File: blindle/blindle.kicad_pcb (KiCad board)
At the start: 2 copper layers, 21 parts, among them J1 CONN_5V, J2 CONN_8V, M1 74HC595, P1 pololua4988, P2 pololua4988, P3 pololua4988, P4 pololua4988, P5 pololua4988, P6 pololua4988, P7 pololua4988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

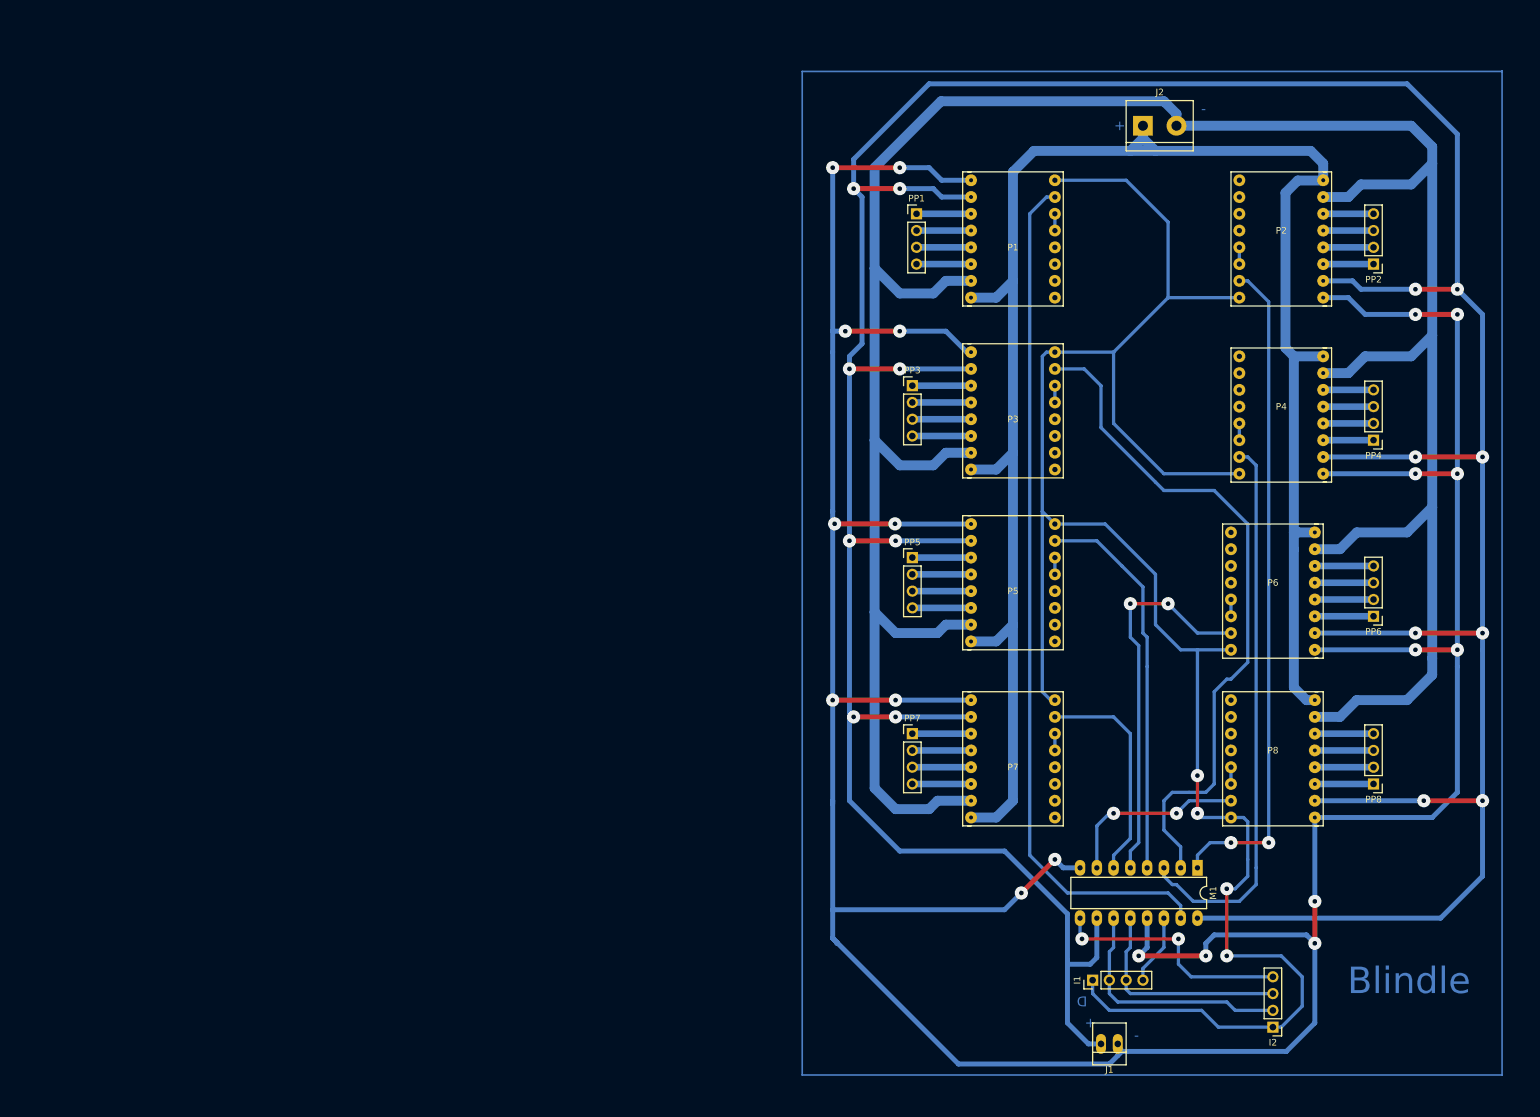
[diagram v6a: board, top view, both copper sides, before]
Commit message: version para placa mas chica
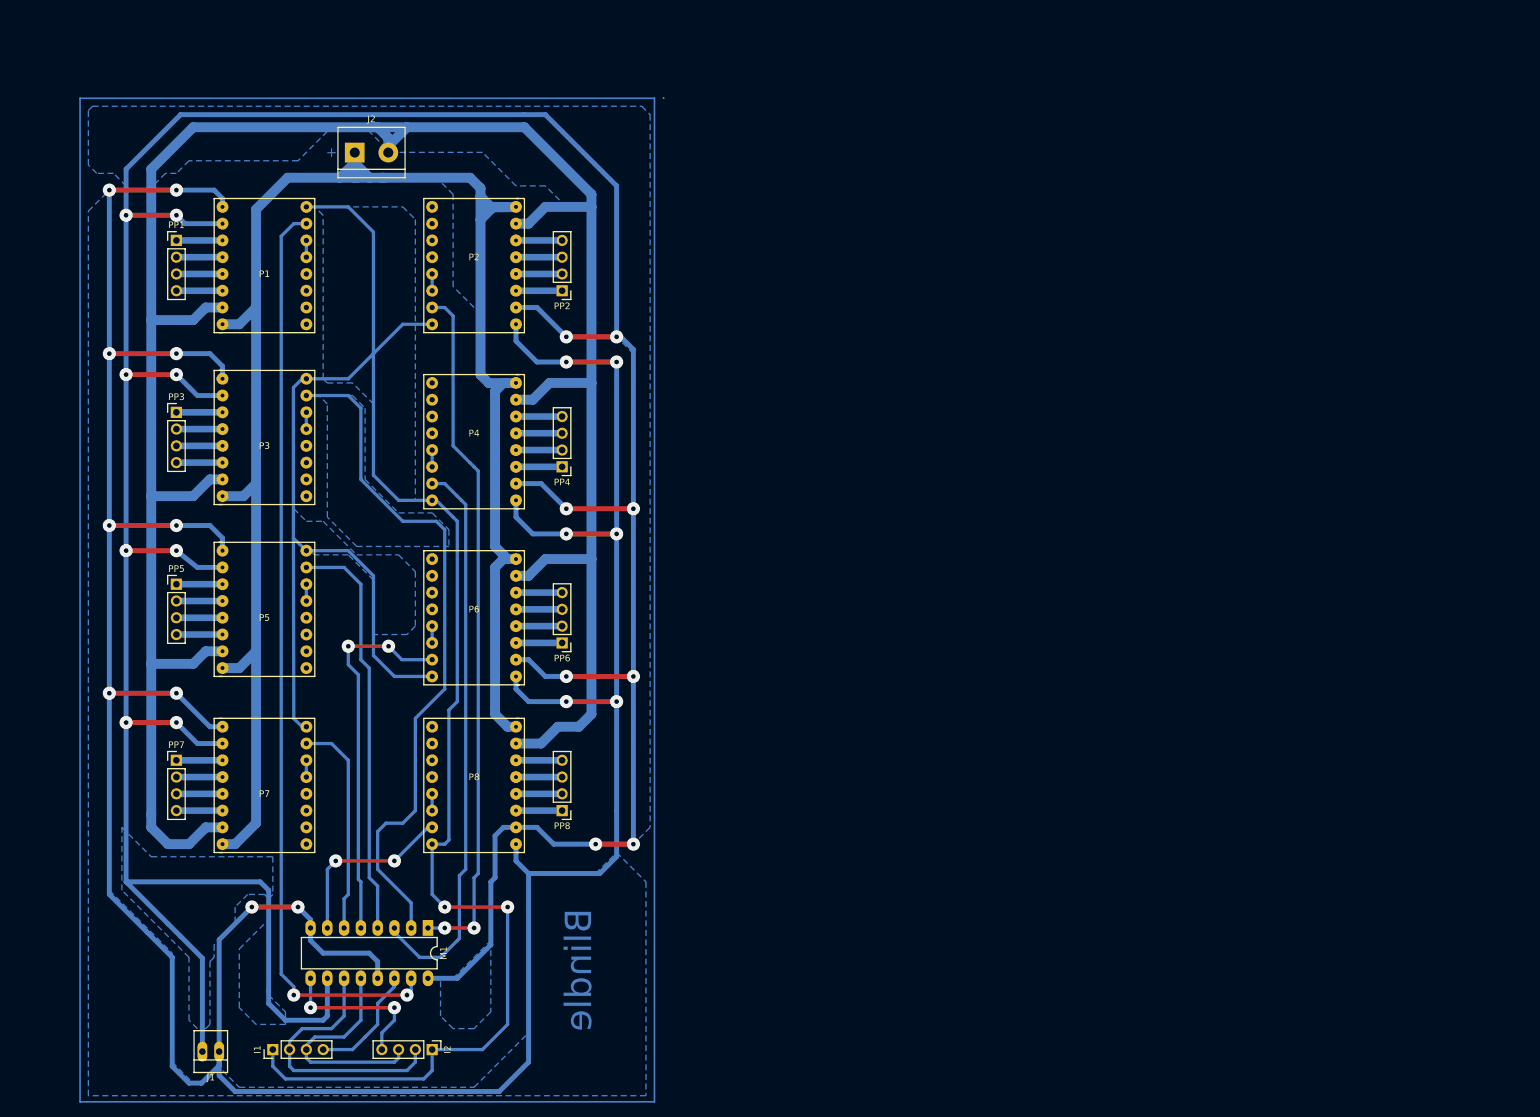
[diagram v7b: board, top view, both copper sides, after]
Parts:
- moved J1 136.1 mm to (68.1, 172.4)
- moved I2 127.4 mm to (100.3, 172.1), turned to 270 degrees
- moved I1 124.6 mm to (76.2, 172.1)
- moved PP2 123.0 mm to (120.0, 57.1)
- moved PP4 123.0 mm to (120.0, 83.8)
- moved PP6 123.0 mm to (120.0, 110.5)
- moved PP8 123.0 mm to (120.0, 135.9)
- moved P2 122.3 mm to (100.3, 44.5)
- moved P4 122.3 mm to (100.3, 71.1)
- moved P6 121.1 mm to (100.3, 97.8)
- moved P8 121.1 mm to (100.3, 123.2)
- moved J2 119.4 mm to (88.6, 36.2)
- moved M1 116.9 mm to (99.7, 153.7)
- moved P1 113.4 mm to (81.3, 62.2)
- moved P3 113.4 mm to (81.3, 88.3)
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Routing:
- net +5V: track 605.5 -> 545.6 mm
- net GNDD: track 411.7 -> 360.7 mm
- net GND: track 557.7 -> 509.7 mm, vias 20 -> 16
- net (no net): track 516.1 -> 478.1 mm
- net Net-(I2-Pad4): track 36.8 -> 24.3 mm
- net Net-(M1-Pad15): track 129.9 -> 140.3 mm, vias 0 -> 2
- net dir: track 302.4 -> 311.8 mm, vias 4 -> 2
- net Net-(I1-Pad4): track 11.9 -> 18.5 mm
- net Net-(M1-Pad1): track 101.2 -> 105.2 mm
- net Net-(M1-Pad4): track 59.0 -> 62.4 mm
- net +8V: track 278.6 -> 275.5 mm
- net Net-(I1-Pad2): track 38.7 -> 41.7 mm
- net Net-(P8-Pad14): track 8.89 -> 6.98 mm
- net Net-(P8-Pad13): track 8.89 -> 6.98 mm
- net Net-(P8-Pad12): track 8.89 -> 6.98 mm
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- added copper zone on B.Cu, net +5V
- added copper zone on B.Cu, net +8V
- added copper zone on B.Cu, net GND
- added copper zone on B.Cu, net GNDD
- added copper zone on B.Cu, net Net-(M1-Pad2)
- added copper zone on B.Cu, net dir
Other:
- board text removed: "-"
- board text removed: "D"

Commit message: cambios menores
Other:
- board text added: "+5v"
- board text added: "+8v"
- board text added: "CK"
- board text added: "DATA"
- board text added: "DATA'"
- board text added: "Dir"
- board text added: "GND"
- board text added: "GNDD"
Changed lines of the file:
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@@
     (area 46.674999 27.644999 135.705002 180.325002)
     (thickness 1.6)
-    (drawings 6)
+    (drawings 24)
     (tracks 454)
     (zones 0)
@@
     (41 Cmts.User user)
     (42 Eco1.User user)
-    (43 Eco2.User user)
-    (44 Edge.Cuts user)
+    (43 Eco2.User user hide)
+    (44 Edge.Cuts user hide)
     (45 Margin user)
-    (46 B.CrtYd user)
+    (46 B.CrtYd user hide)
     (47 F.CrtYd user hide)
     (48 B.Fab user)
@@
     (pad_to_mask_clearance 0.2)
     (aux_axis_origin 0 0)
-    (visible_elements 7FFFFFFF)
+    (visible_elements 7FFCFFFF)
     (pcbplotparams
       (layerselection 0x00030_80000001)
@@
       (net 10 GND))
   )
+  (gr_line (start 47 28) (end 47 180) (angle 90) (layer B.Adhes) (width 0.2))
+  (gr_line (start 134 28) (end 47 28) (angle 90) (layer B.Adhes) (width 0.2))
+  (gr_line (start 134 180) (end 134 28) (angle 90) (layer B.Adhes) (width 0.2))
+  (gr_line (start 47 180) (end 134 180) (angle 90) (layer B.Adhes) (width 0.2))
+  (gr_circle (center 128.778 33.274) (end 124.714 34.544) (layer F.Adhes) (width 0.5))
+  (gr_circle (center 52.578 33.274) (end 50.038 30.226) (layer F.Adhes) (width 0.5))
+  (gr_text +8v (at 83.82 36.195 90) (layer B.Adhes)
+    (effects (font (size 1.5 1.5) (thickness 0.3)) (justify mirror))
+  )
+  (gr_text GNDD (at 98.425 35.56 90) (layer B.Adhes)
+    (effects (font (size 1.5 1.5) (thickness 0.3)) (justify mirror))
+  )
+  (gr_text "GND\n" (at 62.865 172.085 90) (layer B.Adhes)
+    (effects (font (size 1.5 1.5) (thickness 0.3)) (justify mirror))
+  )
+  (gr_text +5v (at 70.485 172.085 90) (layer B.Adhes)
+    (effects (font (size 1.5 1.5) (thickness 0.3)) (justify mirror))
+  )
+  (gr_text CK (at 95.25 175.26 90) (layer B.Adhes)
+    (effects (font (size 1.5 1.5) (thickness 0.3)) (justify mirror))
+  )
+  (gr_text Dir (at 100.33 175.26 90) (layer B.Adhes)
+    (effects (font (size 1.5 1.5) (thickness 0.3)) (justify mirror))
+  )
+  (gr_text CK (at 81.28 175.26 90) (layer B.Adhes)
+    (effects (font (size 1.5 1.5) (thickness 0.3)) (justify mirror))
+  )
+  (gr_text CK (at 78.74 175.26 90) (layer B.Adhes)
+    (effects (font (size 1.5 1.5) (thickness 0.3)) (justify mirror))
+  )
+  (gr_text DATA' (at 92.71 176.53 90) (layer B.Adhes)
+    (effects (font (size 1.5 1.5) (thickness 0.3)) (justify mirror))
+  )
+  (gr_text DATA (at 83.82 176.53 90) (layer B.Adhes)
+    (effects (font (size 1.5 1.5) (thickness 0.3)) (justify mirror))
+  )
+  (gr_text CK (at 97.79 175.26 90) (layer B.Adhes)
+    (effects (font (size 1.5 1.5) (thickness 0.3)) (justify mirror))
+  )
+  (gr_text Dir (at 76.2 175.26 90) (layer B.Adhes)
+    (effects (font (size 1.5 1.5) (thickness 0.3)) (justify mirror))
+  )
   (gr_text + (at 85.09 36.195) (layer B.Cu)
     (effects (font (size 1.5 1.5) (thickness 0.3)) (justify mirror))
@@
     (effects (font (size 4 4) (thickness 1)) (justify mirror))
   )
-  (gr_circle (center 128.84 33.27) (end 130.84 32.27) (layer B.Adhes) (width 1))
-  (gr_circle (center 52.43 33.27) (end 50.43 32.27) (layer B.Adhes) (width 1))
-  (gr_circle (center 52.43 174.73) (end 50.43 175.73) (layer B.Adhes) (width 1))
-  (gr_circle (center 128.84 174.73) (end 127.84 176.73) (layer B.Adhes) (width 1))
+  (gr_circle (center 128.84 33.27) (end 130.84 32.27) (layer F.Adhes) (width 1))
+  (gr_circle (center 52.43 33.27) (end 50.43 32.27) (layer F.Adhes) (width 1))
+  (gr_circle (center 52.43 174.73) (end 50.43 175.73) (layer F.Adhes) (width 1))
+  (gr_circle (center 128.84 174.73) (end 127.84 176.73) (layer F.Adhes) (width 1))
   (segment (start 47 180) (end 134 180) (width 0.25) (layer B.Cu) (net 0))
   (segment (start 47 28) (end 47 180) (width 0.25) (layer B.Cu) (net 0))
@@
     )
   )
-  (zone (net 0) (net_name "") (layer B.Cu) (hatch edge 0.508)
-    (connect_pads (clearance 0.508))
-    (min_thickness 0.254)
-    (keepout (tracks not_allowed) (vias not_allowed) (copperpour not_allowed))
-    (fill (arc_segments 16) (thermal_gap 0.508) (thermal_bridge_width 0.508))
-    (polygon
-      (pts
-        (xy 54.61 34.925) (xy 50.165 34.925) (xy 50.165 31.75) (xy 54.61 31.75)
-      )
-    )
-  )
-  (zone (net 0) (net_name "") (layer B.Cu) (hatch edge 0.508)
-    (connect_pads (clearance 0.508))
-    (min_thickness 0.254)
-    (keepout (tracks not_allowed) (vias not_allowed) (copperpour not_allowed))
-    (fill (arc_segments 16) (thermal_gap 0.508) (thermal_bridge_width 0.508))
-    (polygon
-      (pts
-        (xy 130.81 35.306) (xy 127 35.306) (xy 127 31.496) (xy 130.81 31.496)
-      )
-    )
-  )
-  (zone (net 0) (net_name "") (layer B.Cu) (hatch edge 0.508)
-    (connect_pads (clearance 0.508))
-    (min_thickness 0.254)
-    (keepout (tracks not_allowed) (vias not_allowed) (copperpour not_allowed))
-    (fill (arc_segments 16) (thermal_gap 0.508) (thermal_bridge_width 0.508))
-    (polygon
-      (pts
-        (xy 130.81 176.53) (xy 127 176.53) (xy 127 172.72) (xy 130.81 172.72)
-      )
-    )
-  )
   (zone (net 6) (net_name +5V) (layer B.Cu) (hatch edge 0.508)
     (connect_pads (clearance 0.508))
@@
       )
     )
+  )
+  (zone (net 0) (net_name "") (layer B.Cu) (hatch edge 0.508)
+    (connect_pads (clearance 0.508))
+    (min_thickness 0.254)
+    (keepout (tracks not_allowed) (vias not_allowed) (copperpour not_allowed))
+    (fill (arc_segments 16) (thermal_gap 0.508) (thermal_bridge_width 0.508))
+    (polygon
+      (pts
+        (xy 130.81 176.53) (xy 127 176.53) (xy 127 172.72) (xy 130.81 172.72)
+      )
+    )
+  )
+  (zone (net 0) (net_name "") (layer B.Cu) (hatch edge 0.508)
+    (connect_pads (clearance 0.508))
+    (min_thickness 0.254)
+    (keepout (tracks not_allowed) (vias not_allowed) (copperpour not_allowed))
+    (fill (arc_segments 16) (thermal_gap 0.508) (thermal_bridge_width 0.508))
+    (polygon
+      (pts
+        (xy 56.388 31.75) (xy 56.388 34.544) (xy 53.848 37.084) (xy 51.308 37.084) (xy 48.006 33.782)
+        (xy 48.006 28.956) (xy 53.594 28.956)
+      )
+    )
+  )
+  (zone (net 0) (net_name "") (layer B.Cu) (hatch edge 0.508)
+    (connect_pads (clearance 0.508))
+    (min_thickness 0.254)
+    (keepout (tracks not_allowed) (vias not_allowed) (copperpour not_allowed))
+    (fill (arc_segments 16) (thermal_gap 0.508) (thermal_bridge_width 0.508))
+    (polygon
+      (pts
+        (xy 133.096 34.544) (xy 130.556 37.338) (xy 127 37.338) (xy 124.714 35.052) (xy 124.714 31.242)
+        (xy 127 28.956) (xy 133.096 28.956)
+      )
+    )
